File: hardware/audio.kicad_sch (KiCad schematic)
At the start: 11 parts, among them U8 NS4263_C2829094

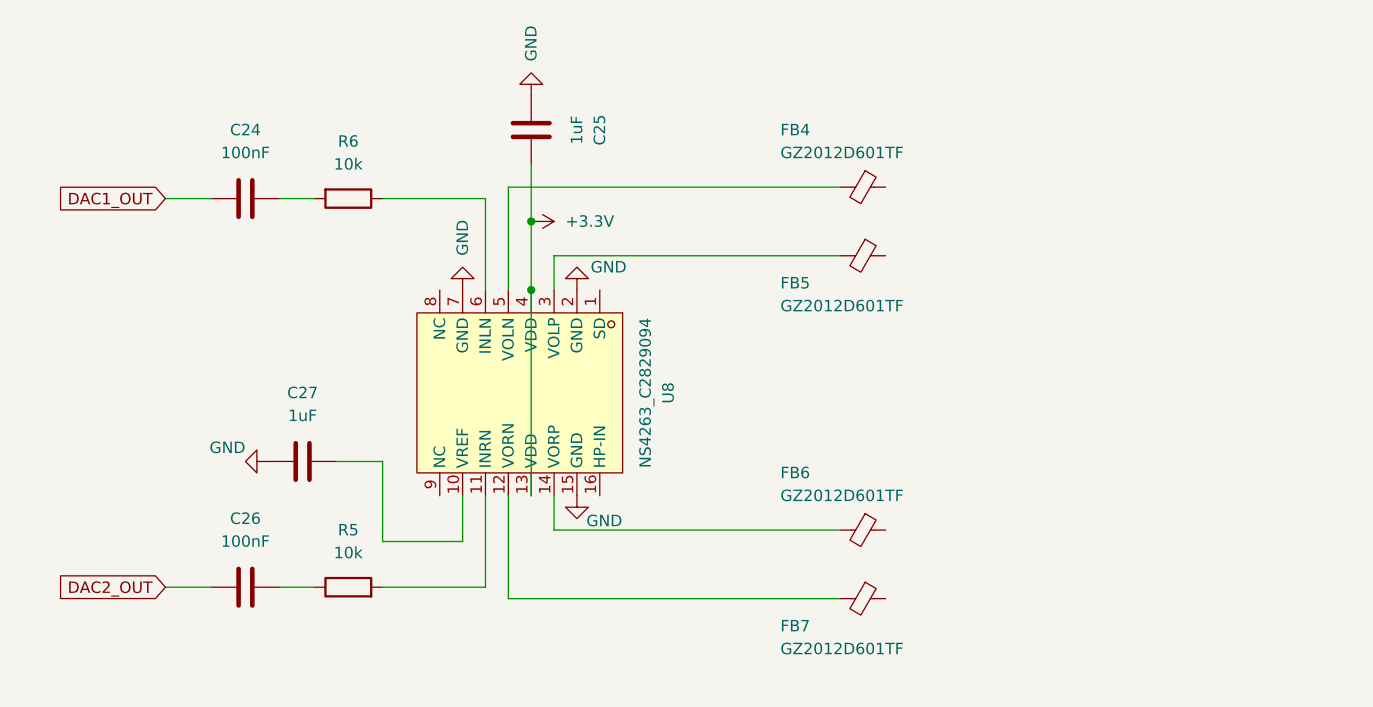
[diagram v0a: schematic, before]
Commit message: initial component layout
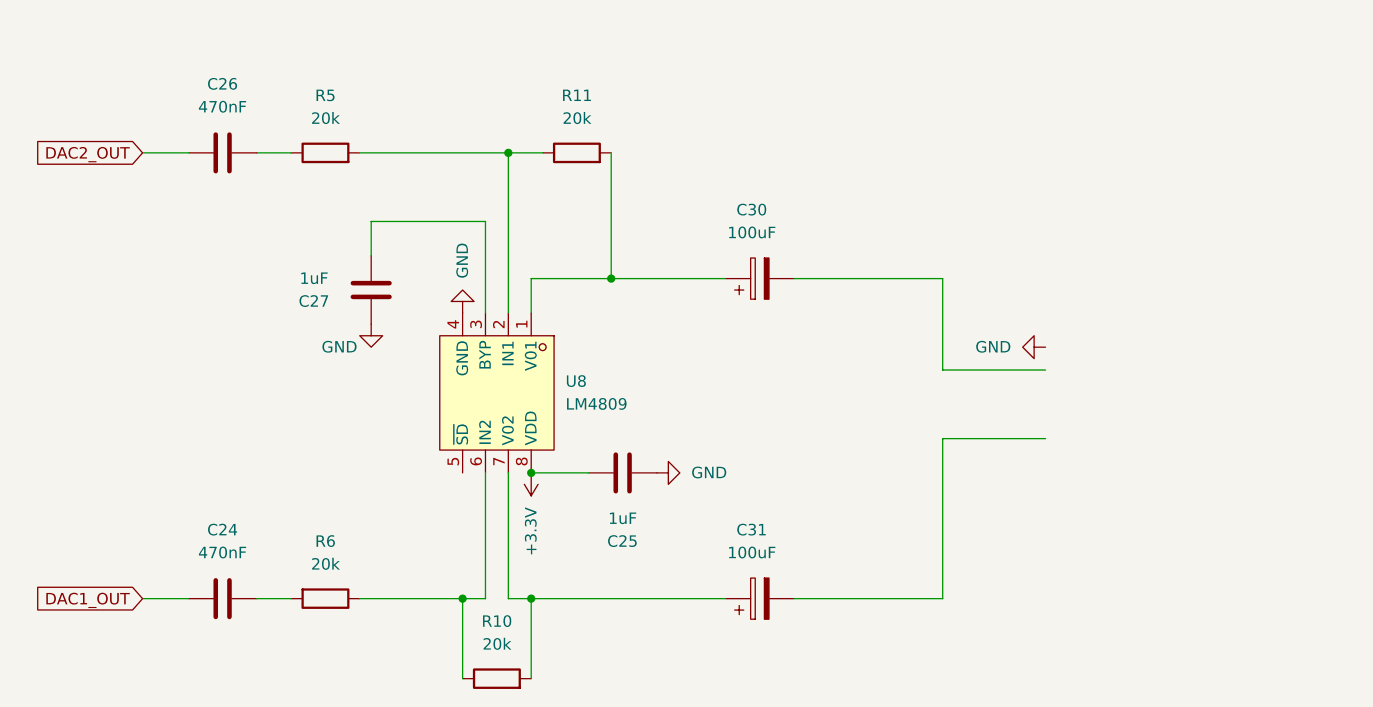
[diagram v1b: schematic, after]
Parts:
- removed FB4, FB5, FB6, FB7: GZ2012D601TF, Inductor_SMD:L_0805_2012Metric_Pad1.05x1.20mm_HandSolder, symbol Device:FerriteBead_Small
- removed U8: NS4263_C2829094, easyeda:SOIC-16_L9.9-W3.9-P1.27-LS6.0-BL, symbol easyeda:NS4263_C2829094
- added C30, C31: 100uF, Capacitor_Tantalum_SMD:CP_EIA-3528-15_AVX-H_HandSolder, symbol Device:C_Polarized
- added R10, R11: 20k, Resistor_SMD:R_0805_2012Metric_Pad1.20x1.40mm_HandSolder, symbol Device:R
- added U8: LM4809, easyeda:MSOP-8_L3.0-W3.0-P0.65-LS4.9-BL, symbol easyeda:LM4809
- C24, C26: value 100nF -> 470nF
- R5, R6: value 10k -> 20k
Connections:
- net +3.3V: now also U8.8 (VDD)
- net GND: now also U8.4 (GND)
- net at C27.1: now also U8.3 (BYP)
- net at R5.2: now also R11.1, U8.2 (IN1)
- net at R6.1: now also R10.1, U8.6 (IN2)
- new net: C31.1, R10.2, U8.7 (V02)
- new net: C30.1, R11.2, U8.1 (V01)
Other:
- moved on the sheet: C24, C25, C26, C27, R5, R6

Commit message: feat: rough routing and features
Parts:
- added J2: AudioPlug4, Connector_Audio:Jack_3.5mm_KoreanHropartsElec_PJ-320D-4A_Horizontal, symbol Connector_Audio:AudioPlug4
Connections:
- net GND: now also J2.R2
- net at C30.2: now also J2.T
- net at C31.2: now also J2.R1
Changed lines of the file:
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@@
 	(wire
 		(pts
-			(xy 158.75 116.84) (xy 158.75 99.06)
+			(xy 158.75 116.84) (xy 158.75 93.98)
 		)
 		(stroke
@@
 	(wire
 		(pts
+			(xy 168.91 96.52) (xy 176.53 96.52)
+		)
+		(stroke
+			(width 0)
+			(type default)
+		)
+	)
+	(wire
+		(pts
 			(xy 110.49 102.87) (xy 110.49 116.84)
 		)
@@
 	(wire
 		(pts
-			(xy 158.75 91.44) (xy 170.18 91.44)
+			(xy 158.75 91.44) (xy 176.53 91.44)
 		)
 		(stroke
@@
 	(wire
 		(pts
-			(xy 158.75 99.06) (xy 170.18 99.06)
+			(xy 158.75 93.98) (xy 176.53 93.98)
 		)
 		(stroke
@@
 	(symbol
 		(lib_id "power:GND")
-		(at 170.18 88.9 270)
+		(at 168.91 96.52 0)
+		(mirror y)
 		(unit 1)
 		(exclude_from_sim no)
@@
 		(dnp no)
 		(property "Reference" "#PWR037"
-			(at 163.83 88.9 0)
+			(at 168.91 102.87 0)
 			(effects
 				(font
@@
 		)
 		(property "Value" "GND"
-			(at 166.37 88.8999 90)
+			(at 168.9101 100.33 90)
 			(effects
 				(font
@@
 		)
 		(property "Footprint" ""
-			(at 170.18 88.9 0)
+			(at 168.91 96.52 0)
 			(effects
 				(font
@@
 		)
 		(property "Datasheet" ""
-			(at 170.18 88.9 0)
+			(at 168.91 96.52 0)
 			(effects
 				(font
@@
 		)
 		(property "Description" "Power symbol creates a global label with name \"GND\" , ground"
-			(at 170.18 88.9 0)
+			(at 168.91 96.52 0)
 			(effects
 				(font
@@
 					(unit 1)
 				)
+			)
+		)
+	)
+	(symbol
+		(lib_id "Connector_Audio:AudioPlug4")
+		(at 191.77 96.52 180)
+		(unit 1)
+		(exclude_from_sim no)
+		(in_bom yes)
+		(on_board yes)
+		(dnp no)
+		(property "Reference" "J2"
+			(at 191.77 105.41 0)
+			(effects
+				(font
+					(size 1.27 1.27)
+				)
+			)
+		)
+		(property "Value" "AudioPlug4"
+			(at 191.77 102.87 0)
+			(effects
+				(font
+					(size 1.27 1.27)
+				)
+			)
+		)
+		(property "Footprint" "Connector_Audio:Jack_3.5mm_KoreanHropartsElec_PJ-320D-4A_Horizontal"
+			(at 182.88 93.98 0)
+			(effects
+				(font
+					(size 1.27 1.27)
+				)
+				(hide yes)
+			)
+		)
+		(property "Datasheet" "~"
+			(at 182.88 93.98 0)
+			(effects
+				(font
+					(size 1.27 1.27)
+				)
+				(hide yes)
+			)
+		)
+		(property "Description" "Audio Jack, 4 Poles (Stereo / TRRS)"
+			(at 191.77 96.52 0)
+			(effects
+				(font
+					(size 1.27 1.27)
+				)
+				(hide yes)
+			)
+		)
+		(pin "T"
+		)
+		(pin "R1"
+		)
+		(pin "S"
+		)
+		(pin "R2"
+		)
+		(instances
+			(project "hfsdr"
+				(path "/a11445ed-c3bd-4d1c-a039-1c09b0dceab8/f5294b00-7550-4c54-b9c8-01c9e56568b3"
+					(reference "J2")
+					(unit 1)
+				)

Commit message: Ready for production
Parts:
- C24, C26: value 470nF -> 1uF
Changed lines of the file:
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@@
 			)
 		)
-		(property "Value" "470nF"
+		(property "Value" "1uF"
 			(at 78.74 111.76 90)
 			(effects
@@
 			)
 		)
-		(property "Value" "470nF"
+		(property "Value" "1uF"
 			(at 78.74 62.23 90)
 			(effects

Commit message: production
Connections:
- net PA11: now reaches U8.5 (~{SD})
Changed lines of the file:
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@@
+		)
+	)
+	(global_label "PA11"
+		(shape input)
+		(at 105.41 102.87 270)
+		(fields_autoplaced yes)
+		(effects
+			(font
+				(size 1.27 1.27)
+			)
+			(justify right)
+		)
+		(property "Intersheetrefs" "${INTERSHEET_REFS}"
+			(at 105.41 110.6328 90)
+			(effects
+				(font
+					(size 1.27 1.27)
+				)
+				(justify right)
+				(hide yes)
+			)
 		)
 	)
